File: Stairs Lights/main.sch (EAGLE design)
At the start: 45 parts, among them IC1 74LS595N, IC2 74LS595N, Q1 2N7000, Q10 2N7000, Q11 2N7000, Q12 2N7000, Q13 2N7000, Q14 2N7000, Q15 2N7000, Q16 2N7000, Q2 2N7000, Q3 2N7000, Q4 2N7000, Q5 2N7000, Q6 2N7000, Q7 2N7000, Q8 2N7000, Q9 2N7000

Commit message: Updated to version 1.2
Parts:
- added C1, C2: (no value), SparkFun:CAPKIT
- added IC3: (no value), SparkFun:V_REG_78XXSINK
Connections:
- net 12V: now also C1.1, IC3.IN
- net GND: now also C1.2, C2.2, IC3.GND
- net VCC: now also C2.1, IC3.OUT
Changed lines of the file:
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@@
 <part name="GND26" library="SparkFun" deviceset="GND" device=""/>
 <part name="POWER" library="SparkFun" deviceset="M02" device="5MM"/>
+<part name="IC3" library="SparkFun" deviceset="V_REG_78XX" device="SINK"/>
+<part name="C1" library="SparkFun" deviceset="CAP" device="KIT"/>
+<part name="C2" library="SparkFun" deviceset="CAP" device="KIT"/>
+<part name="GND27" library="SparkFun" deviceset="GND" device=""/>
+<part name="GND28" library="SparkFun" deviceset="GND" device=""/>
+<part name="U$4" library="com.andrew.eagleLibrary" deviceset="12V" device=""/>
+<part name="P+8" library="SparkFun" deviceset="VCC" device=""/>
 </parts>
 <sheets>
@@
 <instance part="GND26" gate="1" x="-15.24" y="25.4" rot="R90"/>
 <instance part="POWER" gate="G$1" x="-33.02" y="106.68"/>
+<instance part="IC3" gate="G$1" x="27.94" y="7.62"/>
+<instance part="C1" gate="G$1" x="15.24" y="0"/>
+<instance part="C2" gate="G$1" x="40.64" y="0"/>
+<instance part="GND27" gate="1" x="15.24" y="-7.62"/>
+<instance part="GND28" gate="1" x="40.64" y="-7.62"/>
+<instance part="U$4" gate="G$1" x="15.24" y="17.78"/>
+<instance part="P+8" gate="1" x="40.64" y="12.7"/>
 </instances>
 <busses>
@@
 <wire x1="-25.4" y1="30.48" x2="-20.32" y2="30.48" width="0.1524" layer="91"/>
 </segment>
+<segment>
+<pinref part="P+8" gate="1" pin="VCC"/>
+<pinref part="C2" gate="G$1" pin="1"/>
+<wire x1="40.64" y1="12.7" x2="40.64" y2="7.62" width="0.1524" layer="91"/>
+<pinref part="IC3" gate="G$1" pin="OUT"/>
+<wire x1="40.64" y1="7.62" x2="40.64" y2="5.08" width="0.1524" layer="91"/>
+<wire x1="35.56" y1="7.62" x2="40.64" y2="7.62" width="0.1524" layer="91"/>
+</segment>
 </net>
 <net name="GND" class="0">
@@
 <pinref part="POWER" gate="G$1" pin="1"/>
 <pinref part="GND21" gate="1" pin="GND"/>
+</segment>
+<segment>
+<pinref part="C1" gate="G$1" pin="2"/>
+<pinref part="GND27" gate="1" pin="GND"/>
+<wire x1="15.24" y1="-2.54" x2="15.24" y2="-5.08" width="0.1524" layer="91"/>
+<pinref part="IC3" gate="G$1" pin="GND"/>
+<wire x1="27.94" y1="0" x2="27.94" y2="-2.54" width="0.1524" layer="91"/>
+<wire x1="27.94" y1="-2.54" x2="15.24" y2="-2.54" width="0.1524" layer="91"/>
+</segment>
+<segment>
+<pinref part="C2" gate="G$1" pin="2"/>
+<pinref part="GND28" gate="1" pin="GND"/>
+<wire x1="40.64" y1="-2.54" x2="40.64" y2="-5.08" width="0.1524" layer="91"/>
 </segment>
 </net>
@@
 <wire x1="-15.24" y1="109.22" x2="-15.24" y2="116.84" width="0.1524" layer="91"/>
 </segment>
-</net>
+<segment>
+<pinref part="U$4" gate="G$1" pin="12V"/>
+<pinref part="C1" gate="G$1" pin="1"/>
+<wire x1="15.24" y1="12.7" x2="15.24" y2="7.62" width="0.1524" layer="91"/>
+<pinref part="IC3" gate="G$1" pin="IN"/>
+<wire x1="15.24" y1="7.62" x2="15.24" y2="5.08" width="0.1524" layer="91"/>
+<wire x1="15.24" y1="7.62" x2="20.32" y2="7.62" width="0.1524" layer="91"/>
+</segment>
+</net>

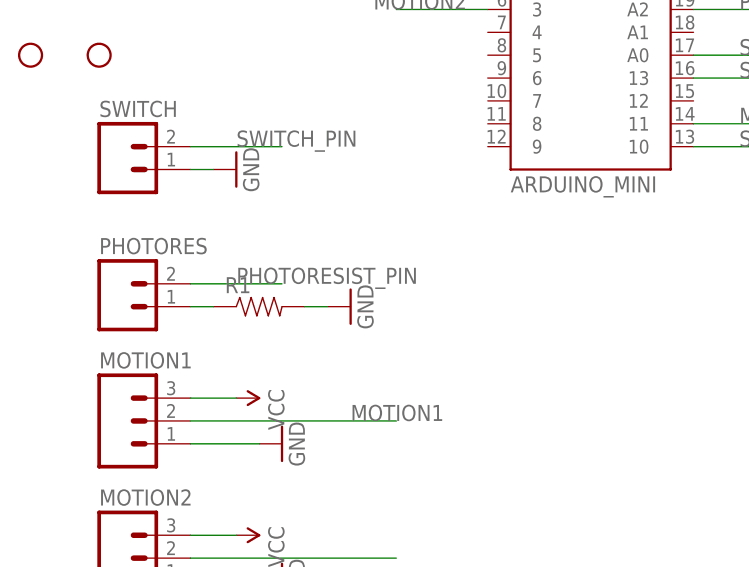
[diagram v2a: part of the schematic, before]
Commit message: 1.3 Fixed photoresistor hardware problem
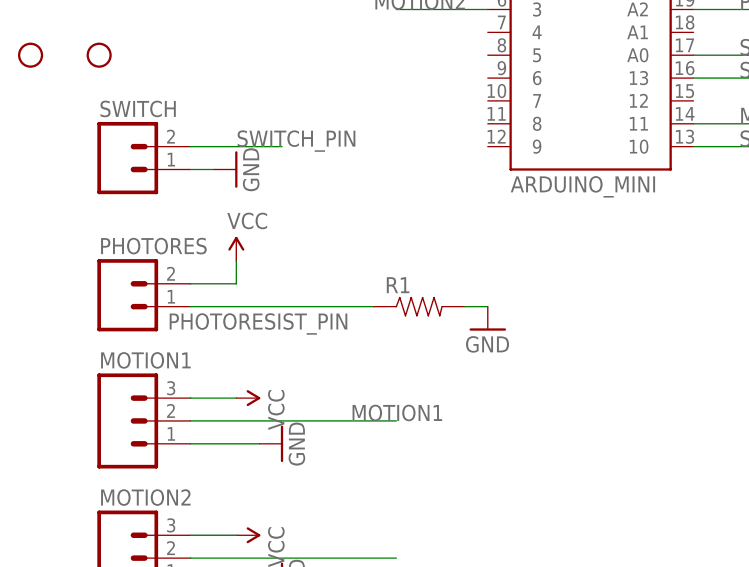
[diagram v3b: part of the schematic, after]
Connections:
- removed net N$22: PHOTORES.1, R1.1
- net PHOTORESIST_PIN: now also PHOTORES.1, R1.1; no longer PHOTORES.2
- net VCC: now also PHOTORES.2
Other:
- moved on the sheet: R1
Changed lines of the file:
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@@
 <?xml version="1.0" encoding="utf-8"?>
 <!DOCTYPE eagle SYSTEM "eagle.dtd">
-<eagle version="6.5.0">
+<eagle version="7.3.0">
 <drawing>
 <settings>
@@
 <part name="U$4" library="com.andrew.eagleLibrary" deviceset="12V" device=""/>
 <part name="P+8" library="SparkFun" deviceset="VCC" device=""/>
+<part name="P+9" library="SparkFun" deviceset="VCC" device=""/>
 </parts>
 <sheets>
@@
 <instance part="GND18" gate="1" x="149.86" y="22.86" rot="R90"/>
 <instance part="GND19" gate="1" x="149.86" y="12.7" rot="R90"/>
-<instance part="GND20" gate="1" x="-7.62" y="55.88" rot="R90"/>
+<instance part="GND20" gate="1" x="7.62" y="53.34"/>
 <instance part="GND21" gate="1" x="-22.86" y="106.68" rot="R90"/>
 <instance part="U$5" gate="G$1" x="-15.24" y="121.92"/>
@@
 <instance part="SWITCH" gate="G$1" x="-33.02" y="71.12"/>
 <instance part="PHOTORES" gate="G$1" x="-33.02" y="55.88"/>
-<instance part="R1" gate="G$1" x="-17.78" y="55.88"/>
+<instance part="R1" gate="G$1" x="0" y="55.88"/>
 <instance part="GND24" gate="1" x="-20.32" y="71.12" rot="R90"/>
 <instance part="MOTION1" gate="G$1" x="-33.02" y="43.18"/>
@@
 <instance part="U$4" gate="G$1" x="15.24" y="17.78"/>
 <instance part="P+8" gate="1" x="40.64" y="12.7"/>
+<instance part="P+9" gate="1" x="-20.32" y="60.96"/>
 </instances>
 <busses>
@@
 <wire x1="35.56" y1="7.62" x2="40.64" y2="7.62" width="0.1524" layer="91"/>
 </segment>
+<segment>
+<pinref part="P+9" gate="1" pin="VCC"/>
+<pinref part="PHOTORES" gate="G$1" pin="2"/>
+<wire x1="-20.32" y1="60.96" x2="-20.32" y2="58.42" width="0.1524" layer="91"/>
+<wire x1="-20.32" y1="58.42" x2="-25.4" y2="58.42" width="0.1524" layer="91"/>
+</segment>
 </net>
 <net name="GND" class="0">
@@
 <pinref part="R1" gate="G$1" pin="2"/>
 <pinref part="GND20" gate="1" pin="GND"/>
-<wire x1="-12.7" y1="55.88" x2="-10.16" y2="55.88" width="0.1524" layer="91"/>
+<wire x1="7.62" y1="55.88" x2="5.08" y2="55.88" width="0.1524" layer="91"/>
 </segment>
 <segment>
@@
 </segment>
 </net>
-<net name="N$22" class="0">
-<segment>
-<pinref part="PHOTORES" gate="G$1" pin="1"/>
-<pinref part="R1" gate="G$1" pin="1"/>
-<wire x1="-25.4" y1="55.88" x2="-22.86" y2="55.88" width="0.1524" layer="91"/>
-</segment>
-</net>
 <net name="PHOTORESIST_PIN" class="0">
-<segment>
-<pinref part="PHOTORES" gate="G$1" pin="2"/>
-<wire x1="-25.4" y1="58.42" x2="-15.24" y2="58.42" width="0.1524" layer="91"/>
-<label x="-20.32" y="58.42" size="1.778" layer="95"/>
-</segment>
 <segment>
 <pinref part="U$1" gate="G$1" pin="A2"/>
@@
 <label x="35.56" y="88.9" size="1.778" layer="95"/>
 </segment>
-</net>
+<segment>
+<pinref part="PHOTORES" gate="G$1" pin="1"/>
+<pinref part="R1" gate="G$1" pin="1"/>
+<wire x1="-25.4" y1="55.88" x2="-5.08" y2="55.88" width="0.1524" layer="91"/>
+<label x="-27.94" y="53.34" size="1.778" layer="95"/>
+</segment>
+</net>
